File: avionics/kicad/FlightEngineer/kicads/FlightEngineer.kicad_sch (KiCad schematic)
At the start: 142 parts

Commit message: feat(avionics): FlightEngineer schematic-first rebuild to ERC 0; PCB placed, DRC 31 open
Replaces FlightEngineer's legacy schematic/PCB (586 ERC violations, PCB pad
nets not matching the schematic at all, gen_flight_engineer.py itself confirmed
drifted per its own injector script's warning) with a fresh generator
pipeline matching Pilot/XO's method (gen_fe_sch.py / gen_fe_footprints.py /
gen_fe_pcb.py), transcribing every pin table from its own OEM datasheet.

Power path: TPS54620 x2 (dual-redundant diode-OR'd 5V BEC) + TPS54540 (6V
BEC), INA226 x5 (main bus + 4 ESC branches), BQ76930 6S cell monitor (Table
9-3 6-cell tap configuration). Trust module rebuilt to the CURRENT target per
FlightEngineer.md's own 2026-08-03 retarget note (MSPM0G3518-Q1 RHB-32 + real
SLB9672 + ISOW1044BDFMR + ISOW1412DFMR), not the superseded MSPM0G3507/
SLB9670 the old injector script still names; the RHB-32 pinmux is reused
verbatim from retarget_mspm0g351x_slb9672.py's own already-verified
FLIGHT_ENGINEER_REMAP/FLIGHT_ENGINEER_TPM_NETS tables rather than re-derived
from the 1500-line datasheet pin-attribute table. ISOW1412's EN/FLT pin is
now wired to a real MCU GPIO (RS485_FLT_N) instead of Pilot's hard-tied
convention, since the RHB-32 pinmux happened to free one.

One part-number defect found in FlightEngineer.md's own BOM and corrected
(flagged, not silently fixed): "AON6556" (Q_BATT_DSG, cited 60V/30A) does not
exist in AOSMD's catalog (their 30V AlphaMOS family tops out at AON6554/
6558; no 60V "6556" found) — substituted with AON6260, a real AOSMD 60V/85A
DFN5x6 MOSFET; NEEDS owner confirmation. MBRD1045CT and SMBJ33CA are
confirmed real via manufacturer/distributor catalog search but their
datasheet PDFs could not be fetched this pass (every mirror returned an HTML
block page) — standard package pinouts used, flagged for a follow-up fetch.

ERC 0 confirmed (kicad-cli sch erc --severity-all, 151 parts, 539 pins).

PCB: courtyard area was budgeted BEFORE layout per docs/solutions/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
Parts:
- removed C1, C2: Panasonic EEF-CX1V221R 220uF/35V, symbol C_Generic
- removed C3: 100nF X7R 0805 50V, symbol C_Generic
- removed CM1, CM2: Wurth 7440640500 10A 2x100uH, symbol CMC_7440640500
- removed CM_ESC1, CM_ESC2, CM_ESC3, CM_ESC4, CM_ESC5: Wurth 7440640500 10A 2x100uH per-ESC CMC, symbol CMC_7440640500
- removed C_5V_OUT: 100nF X7R 0805, symbol C_Generic
- removed C_BEC1_IN, C_BEC2_IN, C_BEC_SV_IN: 100uF/50V electrolytic, symbol C_Generic
- removed C_BEC1_OUT, C_BEC2_OUT, C_BEC_SV_OUT: 220uF 10V electrolytic + 100nF X7R, symbol C_Generic
- removed C_BOOT1, C_BOOT2, C_BOOT_SV: 100nF X7R (BOOT-SW), symbol C_Generic
- removed C_CAP: 4.7uF X7R 0603 BQ76930 boot cap, symbol C_Generic
- removed C_COMP2_SV, C_COMPB1, C_COMPB2: C comp2 hi-f pole (verify per TPS54620 DS), symbol C_Generic
- removed C_COMPA1, C_COMPA2, C_COMP_SV: C comp (verify per TPS54620 DS), symbol C_Generic
- removed C_DEC1, C_DEC2, C_DEC3, C_DEC4, C_DEC5: Panasonic EEUFC1V471 470uF/35V D10x20mm low-ESR, symbol C_Generic
- removed C_DM1: Wurth 885012207016 10uF/50V X7R 1210, symbol C_Generic
- removed C_H_ADM1, C_H_ADM2, C_H_ISO1, C_H_TPM1: 100nF, symbol C_Generic
- removed C_H_IN: 10uF, symbol C_Generic
- removed C_H_ISO2, C_H_VCORE: 1uF, symbol C_Generic
- removed C_H_OUT: 22uF, symbol C_Generic
- removed C_NTC: 100nF X7R 0805 BQ76930 TS1 filter, symbol C_Generic
- removed C_SS1, C_SS2, C_SS_SV: 10nF soft-start (verify per TPS54620 DS), symbol C_Generic
- removed C_Y1, C_Y2: Kemet SA305E472MAR 4.7nF/250V Y2, symbol C_Generic
- removed D1: SMBJ33CA 33V/400W TVS, symbol SMBJ33CA
- removed D_I2C: NXP PRTR5V0U2X Dual TVS 5V clamp I2C RF protection, symbol PRTR5V0U2X
- removed D_OR1, D_OR2: MBRD1045CT Dual Schottky 10A/45V, symbol MBRD1045CT
- removed F1: Littelfuse 0297150.ZXNV 150A MAXI, symbol Fuse_MAXI_150A
- removed FB_5V1, FB_5V2, FB_SERVO: Wurth 742792612 600R@100MHz 2A, symbol FB_Generic
- removed F_ESC1, F_ESC2, F_ESC3, F_ESC4, F_ESC5: Littelfuse 0297040.WXNV 40A mini blade, symbol Fuse_Mini_40A
- removed J_5V: Molex Nano-Fit 4P 2.5mm avionics bus, symbol Nano_Fit_4P
- removed J_ALERT: JST-GH SM02B-GHS-TB 2P 1.25mm ALERT to Wash GPIO, symbol Conn_JST_GH_02P
- removed J_BAL: JST XH-7P 2.54mm 6S balance lead, symbol JST_XH_7P
- removed J_BATT: Amass XT60PW-F, symbol XT60PW_F
- removed J_CAN_IN_H: CAN-FD trunk IN (CANH/CANL/GND), symbol Conn_JST_GH_03P
- removed J_CAN_OUT_H: CAN-FD trunk OUT (CANH/CANL/GND), symbol Conn_JST_GH_03P
- removed J_CHASSIS: M3 x8 brass standoff (x4), symbol M3_ChassisPad
- removed J_ESC1, J_ESC2, J_ESC3, J_ESC4, J_ESC5: Amass XT30PW-F PCB-mount XT30 female, symbol XT30PW_F
- removed J_I2C: JST-GH SM04B-GHS-TB 4P 1.25mm PDB I2C to FC1, symbol Conn_JST_GH_04P
- removed J_NTC: JST-GH 2P 1.25mm battery NTC thermistor input, symbol Conn_JST_GH_02P
- removed J_PGND_BATT: M3 chassis lug, symbol M3_ChassisPad
- removed J_RS485_IN_H: RS-485 trunk IN (A/B/GND), symbol Conn_JST_GH_03P
- removed J_RS485_OUT_H: RS-485 trunk OUT (A/B/GND), symbol Conn_JST_GH_03P
- removed J_SERVO_5V: Molex Nano-Fit 4P 2.5mm SERVO-5V bus, symbol Nano_Fit_4P
- removed J_SHLD_5V: PGND via-pad 1.2mm for 5V cable shield, symbol M3_ChassisPad
- removed J_SHLD_ALERT: PGND via-pad ALERT cable shield, symbol M3_ChassisPad
- removed J_SHLD_ESC1, J_SHLD_ESC2, J_SHLD_ESC3, J_SHLD_ESC4, J_SHLD_ESC5: M3 chassis lug for ESC cable shield, symbol M3_ChassisPad
- removed J_SHLD_I2C: PGND via-pad I2C cable shield, symbol M3_ChassisPad
- removed J_SHLD_NTC: PGND via-pad NTC cable shield, symbol M3_ChassisPad
- removed J_SHLD_SV: PGND via-pad for SERVO-5V cable shield, symbol M3_ChassisPad
- removed J_SWD_H: SWD: DIO/CLK/NRST/GND, symbol Conn_JST_GH_04P
- removed L1, L2, L4: Wurth 744314100 10uH >=6A Isat, symbol L_Generic
- removed L_H1: 2.2uH, symbol L_Generic
- removed Q_BATT_DSG: AON6556 60V/30A NMOS, symbol AON6556
- removed RS1, RS2, RS3, RS4, RS5, RS_MAIN: Bourns CSS2H-2512K-1L00F 1mOhm 3W, symbol CSS2H_2512K_1mOhm
- removed R_ALERT: 2.2k 0402 ALERT pull-up to +5V, symbol R_Generic
- removed R_BAL1, R_BAL2, R_BAL3, R_BAL4, R_BAL5, R_BAL6: 100R 0402 balance lead protection resistor, symbol R_Generic
- removed R_CHGND: 0R 0402 (chassis-PGND bond, configurable), symbol R_Generic
- removed R_COMP1, R_COMP2, R_COMP_SV: R comp (verify per TPS54620 DS), symbol R_Generic
- removed R_DSG_G: 10k 0402, symbol R_Generic
- removed R_FB1_1, R_FB2_1: R for Vout=5.3V (top), symbol R_Generic
- removed R_FB1_2, R_FB2_2: R for Vout=5.3V (bot), symbol R_Generic
- removed R_FBSV_1: R for Vout=5.0V (top), symbol R_Generic
- removed R_FBSV_2: R for Vout=5.0V (bot), symbol R_Generic
- removed R_H_485TERM, R_H_CANTERM: 120R, symbol R_Generic
- removed R_H_FBB: 20k, symbol R_Generic
- removed R_H_FBT, R_H_NRST, R_H_TPM_RST: 10k, symbol R_Generic
- removed R_VSNS: 0R Kelvin VBUS tap (VDIS), symbol R_Generic
- removed SJ_H_485, SJ_H_CAN: open by default, Jumper:SolderJumper-2_P1.3mm_Open_Pad1.0x1.5mm, symbol SJ_Generic
- removed U_BEC_5V_1, U_BEC_5V_2: TPS54620RGYT 6A/28V sync buck 5.3Vout, symbol TPS54620RGYT
- removed U_BEC_SERVO_5V: TPS54620RGYT 6A/28V sync buck 5.0V servo rail, symbol TPS54620RGYT
- removed U_CELL: BQ76930PWRQ1 6S cell monitor + HW protection, symbol BQ76930PWRQ1
- removed U_IS1: INA226AIDGSR I2C addr=0x40, symbol INA226AIDGSR
- removed U_IS2: INA226AIDGSR I2C addr=0x41, symbol INA226AIDGSR
- removed U_IS3: INA226AIDGSR I2C addr=0x42, symbol INA226AIDGSR
- removed U_IS4: INA226AIDGSR I2C addr=0x43, symbol INA226AIDGSR
- removed U_IS5: INA226AIDGSR I2C addr=0x45, symbol INA226AIDGSR
- removed U_ISOCAN: TI ISOW1044BDFMR, Package_SO:SOIC-20W_7.5x12.8mm_P1.27mm, symbol Observer_ISOW1044BDFMR
- removed U_IS_MAIN: INA226AIDGSR I2C addr=0x44, symbol INA226AIDGSR
- removed U_MCU: TI MSPM0G3518-Q1, Package_DFN_QFN:Texas_RHB0032E_VQFN-32-1EP_5x5mm_P0.5mm_EP3.45x3.45mm, symbol MSPM0G3518_Q1_RHB
- removed U_REG_3V3_H: TLV62569DBVR -> +3V3, symbol TLV62569_DBV_H
- removed U_RS485: TI ISOW1412, Package_SO:SOIC-20W_7.5x12.8mm_P1.27mm, symbol GW_ISOW1412
- removed U_TPM: Infineon SLB 9672AU2.0, Package_DFN_QFN:QFN-32-1EP_5x5mm_P0.5mm_EP3.6x3.6mm, symbol SLB9672_TPM
- added C1: 220uF 35V, Capacitor_THT:CP_Radial_D10.0mm_P5.00mm, symbol FlightEngineer:S_C1
- added C2: 220uF 35V, Capacitor_THT:CP_Radial_D10.0mm_P5.00mm, symbol FlightEngineer:S_C2
- added C3: 100nF X7R 0805, Capacitor_SMD:C_0805_2012Metric, symbol FlightEngineer:S_C3
- added CM1: 7440640500, Serenity-Custom:Wurth_7440640500_CMC_THT, symbol FlightEngineer:S_CM1
- added CM2: 7440640500, Serenity-Custom:Wurth_7440640500_CMC_THT, symbol FlightEngineer:S_CM2
- added CM_ESC1: 7440640500, Serenity-Custom:Wurth_7440640500_CMC_THT, symbol FlightEngineer:S_CM_ESC1
- added CM_ESC2: 7440640500, Serenity-Custom:Wurth_7440640500_CMC_THT, symbol FlightEngineer:S_CM_ESC2
- added CM_ESC3: 7440640500, Serenity-Custom:Wurth_7440640500_CMC_THT, symbol FlightEngineer:S_CM_ESC3
- added CM_ESC4: 7440640500, Serenity-Custom:Wurth_7440640500_CMC_THT, symbol FlightEngineer:S_CM_ESC4
- added C_BEC1_BOOT: 100nF, Capacitor_SMD:C_0402_1005Metric, symbol FlightEngineer:S_C_BEC1_BOOT
- added C_BEC1_COMP: 2.2nF, Capacitor_SMD:C_0402_1005Metric, symbol FlightEngineer:S_C_BEC1_COMP
- added C_BEC1_IN: 100uF 50V, Capacitor_SMD:C_1210_3225Metric, symbol FlightEngineer:S_C_BEC1_IN
- added C_BEC1_OUT1: 220uF, Capacitor_SMD:C_1210_3225Metric, symbol FlightEngineer:S_C_BEC1_OUT1
- added C_BEC1_OUT2: 100nF, Capacitor_SMD:C_0402_1005Metric, symbol FlightEngineer:S_C_BEC1_OUT2
- added C_BEC1_SS: 10nF, Capacitor_SMD:C_0402_1005Metric, symbol FlightEngineer:S_C_BEC1_SS
- added C_BEC2_BOOT: 100nF, Capacitor_SMD:C_0402_1005Metric, symbol FlightEngineer:S_C_BEC2_BOOT
- added C_BEC2_COMP: 2.2nF, Capacitor_SMD:C_0402_1005Metric, symbol FlightEngineer:S_C_BEC2_COMP
- added C_BEC2_IN: 100uF 50V, Capacitor_SMD:C_1210_3225Metric, symbol FlightEngineer:S_C_BEC2_IN
- added C_BEC2_OUT1: 220uF, Capacitor_SMD:C_1210_3225Metric, symbol FlightEngineer:S_C_BEC2_OUT1
- added C_BEC2_OUT2: 100nF, Capacitor_SMD:C_0402_1005Metric, symbol FlightEngineer:S_C_BEC2_OUT2
- added C_BEC2_SS: 10nF, Capacitor_SMD:C_0402_1005Metric, symbol FlightEngineer:S_C_BEC2_SS
- added C_BEC6_BOOT: 100nF, Capacitor_SMD:C_0402_1005Metric, symbol FlightEngineer:S_C_BEC6_BOOT
- added C_BEC6_COMP: 1nF, Capacitor_SMD:C_0402_1005Metric, symbol FlightEngineer:S_C_BEC6_COMP
- added C_BEC_SV_IN: 100uF 50V, Capacitor_SMD:C_1210_3225Metric, symbol FlightEngineer:S_C_BEC_SV_IN
- added C_BEC_SV_OUT1: 100uF, Capacitor_SMD:C_1210_3225Metric, symbol FlightEngineer:S_C_BEC_SV_OUT1
- added C_BEC_SV_OUT2: 100nF, Capacitor_SMD:C_0402_1005Metric, symbol FlightEngineer:S_C_BEC_SV_OUT2
- added C_CAP1: 0.1uF, Capacitor_SMD:C_0402_1005Metric, symbol FlightEngineer:S_C_CAP1
- added C_CAP2: 0.1uF, Capacitor_SMD:C_0402_1005Metric, symbol FlightEngineer:S_C_CAP2
- added C_DEC1: 470uF 35V low-ESR, Capacitor_THT:CP_Radial_D10.0mm_P5.00mm, symbol FlightEngineer:S_C_DEC1
- added C_DEC2: 470uF 35V low-ESR, Capacitor_THT:CP_Radial_D10.0mm_P5.00mm, symbol FlightEngineer:S_C_DEC2
- added C_DEC3: 470uF 35V low-ESR, Capacitor_THT:CP_Radial_D10.0mm_P5.00mm, symbol FlightEngineer:S_C_DEC3
- added C_DEC4: 470uF 35V low-ESR, Capacitor_THT:CP_Radial_D10.0mm_P5.00mm, symbol FlightEngineer:S_C_DEC4
- added C_DM1: 10uF 50V X7R 1210, Capacitor_SMD:C_1210_3225Metric, symbol FlightEngineer:S_C_DM1
- added C_H_IN: 10uF, Capacitor_SMD:C_0805_2012Metric, symbol FlightEngineer:S_C_H_IN
- added C_H_OUT: 22uF, Capacitor_SMD:C_0805_2012Metric, symbol FlightEngineer:S_C_H_OUT
- added C_ISOCAN1: 10nF, Capacitor_SMD:C_0402_1005Metric, symbol FlightEngineer:S_C_ISOCAN1
- added C_ISOCAN2: 10uF, Capacitor_SMD:C_0805_2012Metric, symbol FlightEngineer:S_C_ISOCAN2
- added C_ISOCAN3: 100nF, Capacitor_SMD:C_0402_1005Metric, symbol FlightEngineer:S_C_ISOCAN3
- added C_ISOCAN4: 10nF, Capacitor_SMD:C_0402_1005Metric, symbol FlightEngineer:S_C_ISOCAN4
- added C_ISOCAN5: 10uF, Capacitor_SMD:C_0805_2012Metric, symbol FlightEngineer:S_C_ISOCAN5
- added C_MCU_3V3: 100nF, Capacitor_SMD:C_0402_1005Metric, symbol FlightEngineer:S_C_MCU_3V3
- added C_MCU_VCORE: 1uF, Capacitor_SMD:C_0402_1005Metric, symbol FlightEngineer:S_C_MCU_VCORE
- added C_NTC: 100nF X7R, Capacitor_SMD:C_0402_1005Metric, symbol FlightEngineer:S_C_NTC
- added C_REGOUT: 1uF, Capacitor_SMD:C_0402_1005Metric, symbol FlightEngineer:S_C_REGOUT
- added C_RS485_1: 10nF, Capacitor_SMD:C_0402_1005Metric, symbol FlightEngineer:S_C_RS485_1
- added C_RS485_2: 10uF, Capacitor_SMD:C_0805_2012Metric, symbol FlightEngineer:S_C_RS485_2
- added C_RS485_3: 100nF, Capacitor_SMD:C_0402_1005Metric, symbol FlightEngineer:S_C_RS485_3
- added C_RS485_4: 10nF, Capacitor_SMD:C_0402_1005Metric, symbol FlightEngineer:S_C_RS485_4
- added C_RS485_5: 10uF, Capacitor_SMD:C_0805_2012Metric, symbol FlightEngineer:S_C_RS485_5
- added C_TPM1: 1uF, Capacitor_SMD:C_0402_1005Metric, symbol FlightEngineer:S_C_TPM1
- added C_TPM2: 100nF, Capacitor_SMD:C_0402_1005Metric, symbol FlightEngineer:S_C_TPM2
- added C_TPM3: 100nF, Capacitor_SMD:C_0402_1005Metric, symbol FlightEngineer:S_C_TPM3
- added C_TPM4: 100nF, Capacitor_SMD:C_0402_1005Metric, symbol FlightEngineer:S_C_TPM4
- added C_Y1: 4.7nF 250V Y2, Capacitor_SMD:C_0805_2012Metric, symbol FlightEngineer:S_C_Y1
- added C_Y2: 4.7nF 250V Y2, Capacitor_SMD:C_0805_2012Metric, symbol FlightEngineer:S_C_Y2
- added D1: SMBJ33CA, Diode_SMD:D_SMB, symbol FlightEngineer:S_D1
- added D_I2C: PRTR5V0U2X, Package_TO_SOT_SMD:SOT-363_SC-70-6, symbol FlightEngineer:S_D_I2C
- added D_OR1: MBRD1045CT, Package_TO_SOT_SMD:TO-263-3_TabPin2, symbol FlightEngineer:S_D_OR1
- added D_OR2: MBRD1045CT, Package_TO_SOT_SMD:TO-263-3_TabPin2, symbol FlightEngineer:S_D_OR2
- added ESC1_LINK: 0R link, Resistor_SMD:R_0603_1608Metric, symbol FlightEngineer:S_ESC1_LINK
- added ESC2_LINK: 0R link, Resistor_SMD:R_0603_1608Metric, symbol FlightEngineer:S_ESC2_LINK
- added ESC3_LINK: 0R link, Resistor_SMD:R_0603_1608Metric, symbol FlightEngineer:S_ESC3_LINK
- added ESC4_LINK: 0R link, Resistor_SMD:R_0603_1608Metric, symbol FlightEngineer:S_ESC4_LINK
- added F1: 0297150.ZXNV 150A MAXI, Serenity-Custom:MAXI_Blade_Fuseholder_2P, symbol FlightEngineer:S_F1
- added FB_5V1: 742792612, Inductor_SMD:L_1210_3225Metric, symbol FlightEngineer:S_FB_5V1
- added FB_5V2: 742792612, Inductor_SMD:L_1210_3225Metric, symbol FlightEngineer:S_FB_5V2
- added FB_6V: 742792612, Inductor_SMD:L_1210_3225Metric, symbol FlightEngineer:S_FB_6V
- added F_ESC1: 0297040.WXNV 40A mini, Fuse:Fuseholder_Blade_Mini_Keystone_3568, symbol FlightEngineer:S_F_ESC1
- added F_ESC2: 0297040.WXNV 40A mini, Fuse:Fuseholder_Blade_Mini_Keystone_3568, symbol FlightEngineer:S_F_ESC2
- added F_ESC3: 0297040.WXNV 40A mini, Fuse:Fuseholder_Blade_Mini_Keystone_3568, symbol FlightEngineer:S_F_ESC3
- added F_ESC4: 0297040.WXNV 40A mini, Fuse:Fuseholder_Blade_Mini_Keystone_3568, symbol FlightEngineer:S_F_ESC4
- added J_485_IN: SM03B-GHS-TB, Connector_JST:JST_GH_SM03B-GHS-TB_1x03-1MP_P1.25mm_Horizontal, symbol FlightEngineer:S_J_485_IN
- added J_485_OUT: SM03B-GHS-TB, Connector_JST:JST_GH_SM03B-GHS-TB_1x03-1MP_P1.25mm_Horizontal, symbol FlightEngineer:S_J_485_OUT
- added J_5V: Nano-Fit 4P, Connector_Molex:Molex_Nano-Fit_105309-xx04_1x04_P2.50mm_Vertical, symbol FlightEngineer:S_J_5V
- added J_6V: Nano-Fit 4P, Connector_Molex:Molex_Nano-Fit_105309-xx04_1x04_P2.50mm_Vertical, symbol FlightEngineer:S_J_6V
- added J_ALERT: SM02B-GHS-TB, Connector_JST:JST_GH_SM02B-GHS-TB_1x02-1MP_P1.25mm_Horizontal, symbol FlightEngineer:S_J_ALERT
- added J_BAL: XH-7P, Connector_JST:JST_XH_B7B-XH-A_1x07_P2.50mm_Vertical, symbol FlightEngineer:S_J_BAL
- added J_BATT: XT60PW-F, Connector_AMASS:AMASS_XT60PW-F_1x02_P7.20mm_Horizontal, symbol FlightEngineer:S_J_BATT
- added J_CAN_IN: SM03B-GHS-TB, Connector_JST:JST_GH_SM03B-GHS-TB_1x03-1MP_P1.25mm_Horizontal, symbol FlightEngineer:S_J_CAN_IN
- added J_CAN_OUT: SM03B-GHS-TB, Connector_JST:JST_GH_SM03B-GHS-TB_1x03-1MP_P1.25mm_Horizontal, symbol FlightEngineer:S_J_CAN_OUT
- added J_CHASSIS: M3 standoff x4, Serenity-Custom:M3_Chassis_Lug_PGND, symbol FlightEngineer:S_J_CHASSIS
- added J_ESC1: XT30PW-F, Connector_AMASS:AMASS_XT30PW-F_1x02_P2.50mm_Horizontal, symbol FlightEngineer:S_J_ESC1
- added J_ESC2: XT30PW-F, Connector_AMASS:AMASS_XT30PW-F_1x02_P2.50mm_Horizontal, symbol FlightEngineer:S_J_ESC2
- added J_ESC3: XT30PW-F, Connector_AMASS:AMASS_XT30PW-F_1x02_P2.50mm_Horizontal, symbol FlightEngineer:S_J_ESC3
- added J_ESC4: XT30PW-F, Connector_AMASS:AMASS_XT30PW-F_1x02_P2.50mm_Horizontal, symbol FlightEngineer:S_J_ESC4
- added J_I2C: SM04B-GHS-TB, Connector_JST:JST_GH_SM04B-GHS-TB_1x04-1MP_P1.25mm_Horizontal, symbol FlightEngineer:S_J_I2C
- added J_NTC: SM02B-GHS-TB, Connector_JST:JST_GH_SM02B-GHS-TB_1x02-1MP_P1.25mm_Horizontal, symbol FlightEngineer:S_J_NTC
- added J_PGND_BATT: M3 chassis lug, Serenity-Custom:M3_Chassis_Lug_PGND, symbol FlightEngineer:S_J_PGND_BATT
- added J_SHLD_5V: PGND via, Serenity-Custom:PGND_ViaPad_1p2mm, symbol FlightEngineer:S_J_SHLD_5V
- added J_SHLD_6V: PGND via, Serenity-Custom:PGND_ViaPad_1p2mm, symbol FlightEngineer:S_J_SHLD_6V
- added J_SHLD_ALERT: PGND via, Serenity-Custom:PGND_ViaPad_1p2mm, symbol FlightEngineer:S_J_SHLD_ALERT
- added J_SHLD_ESC1: M3 chassis lug, Serenity-Custom:M3_Chassis_Lug_PGND, symbol FlightEngineer:S_J_SHLD_ESC1
- added J_SHLD_ESC2: M3 chassis lug, Serenity-Custom:M3_Chassis_Lug_PGND, symbol FlightEngineer:S_J_SHLD_ESC2
- added J_SHLD_ESC3: M3 chassis lug, Serenity-Custom:M3_Chassis_Lug_PGND, symbol FlightEngineer:S_J_SHLD_ESC3
- added J_SHLD_ESC4: M3 chassis lug, Serenity-Custom:M3_Chassis_Lug_PGND, symbol FlightEngineer:S_J_SHLD_ESC4
- added J_SHLD_I2C: PGND via, Serenity-Custom:PGND_ViaPad_1p2mm, symbol FlightEngineer:S_J_SHLD_I2C
- added J_SHLD_NTC: PGND via, Serenity-Custom:PGND_ViaPad_1p2mm, symbol FlightEngineer:S_J_SHLD_NTC
- added J_SWD_H: SM04B-GHS-TB, Connector_JST:JST_GH_SM04B-GHS-TB_1x04-1MP_P1.25mm_Horizontal, symbol FlightEngineer:S_J_SWD_H
- added L1: 10uH 6A, Inductor_SMD:L_1210_3225Metric, symbol FlightEngineer:S_L1
- added L2: 10uH 6A, Inductor_SMD:L_1210_3225Metric, symbol FlightEngineer:S_L2
- added L3: 10uH 6A, Inductor_SMD:L_1210_3225Metric, symbol FlightEngineer:S_L3
- added L_H1: 2.2uH, Inductor_SMD:L_1210_3225Metric, symbol FlightEngineer:S_L_H1
- added Q_BATT_CHG: AON6260 (DNP), Serenity-Custom:AOSMD_DFN5x6-8L, symbol FlightEngineer:S_Q_BATT_CHG
- added Q_BATT_DSG: AON6260, Serenity-Custom:AOSMD_DFN5x6-8L, symbol FlightEngineer:S_Q_BATT_DSG
- added RS1: 1mOhm 3W Kelvin, Resistor_SMD:R_Shunt_Vishay_WSK2512_6332Metric_T1.19mm, symbol FlightEngineer:S_RS1
- added RS2: 1mOhm 3W Kelvin, Resistor_SMD:R_Shunt_Vishay_WSK2512_6332Metric_T1.19mm, symbol FlightEngineer:S_RS2
- added RS3: 1mOhm 3W Kelvin, Resistor_SMD:R_Shunt_Vishay_WSK2512_6332Metric_T1.19mm, symbol FlightEngineer:S_RS3
- added RS4: 1mOhm 3W Kelvin, Resistor_SMD:R_Shunt_Vishay_WSK2512_6332Metric_T1.19mm, symbol FlightEngineer:S_RS4
- added RS_MAIN: 1mOhm 5W Kelvin, Resistor_SMD:R_Shunt_Vishay_WSK2512_6332Metric_T1.19mm, symbol FlightEngineer:S_RS_MAIN
- added R_485TERM: 120R, Resistor_SMD:R_0603_1608Metric, symbol FlightEngineer:S_R_485TERM
- added R_ALERT: 2.2k, Resistor_SMD:R_0402_1005Metric, symbol FlightEngineer:S_R_ALERT
- added R_BAL1: 100R, Resistor_SMD:R_0402_1005Metric, symbol FlightEngineer:S_R_BAL1
- added R_BAL2: 100R, Resistor_SMD:R_0402_1005Metric, symbol FlightEngineer:S_R_BAL2
- added R_BAL3: 100R, Resistor_SMD:R_0402_1005Metric, symbol FlightEngineer:S_R_BAL3
- added R_BAL4: 100R, Resistor_SMD:R_0402_1005Metric, symbol FlightEngineer:S_R_BAL4
- added R_BAL5: 100R, Resistor_SMD:R_0402_1005Metric, symbol FlightEngineer:S_R_BAL5
- added R_BAL6: 100R, Resistor_SMD:R_0402_1005Metric, symbol FlightEngineer:S_R_BAL6
- added R_CANSTB: 0R, Resistor_SMD:R_0402_1005Metric, symbol FlightEngineer:S_R_CANSTB
- added R_CANTERM: 120R, Resistor_SMD:R_0603_1608Metric, symbol FlightEngineer:S_R_CANTERM
- added R_CHGND: 0R socketed, Resistor_SMD:R_0402_1005Metric, symbol FlightEngineer:S_R_CHGND
- added R_DSG_G: 10k, Resistor_SMD:R_0402_1005Metric, symbol FlightEngineer:S_R_DSG_G
- added R_EN_BIAS: 100k, Resistor_SMD:R_0402_1005Metric, symbol FlightEngineer:S_R_EN_BIAS
- added R_FB1_1: 56.2k 1%, Resistor_SMD:R_0402_1005Metric, symbol FlightEngineer:S_R_FB1_1
- added R_FB1_2: 10.0k 1%, Resistor_SMD:R_0402_1005Metric, symbol FlightEngineer:S_R_FB1_2
- added R_FB2_1: 56.2k 1%, Resistor_SMD:R_0402_1005Metric, symbol FlightEngineer:S_R_FB2_1
- added R_FB2_2: 10.0k 1%, Resistor_SMD:R_0402_1005Metric, symbol FlightEngineer:S_R_FB2_2
- added R_FB6_1: 64.9k 1%, Resistor_SMD:R_0402_1005Metric, symbol FlightEngineer:S_R_FB6_1
- added R_FB6_2: 10.0k 1%, Resistor_SMD:R_0402_1005Metric, symbol FlightEngineer:S_R_FB6_2
- added R_GND_PGND: 0R, Resistor_SMD:R_0603_1608Metric, symbol FlightEngineer:S_R_GND_PGND
- added R_I2C_SCL: 4.7k, Resistor_SMD:R_0402_1005Metric, symbol FlightEngineer:S_R_I2C_SCL
- added R_I2C_SDA: 4.7k, Resistor_SMD:R_0402_1005Metric, symbol FlightEngineer:S_R_I2C_SDA
- added R_MCU_NRST: 10k, Resistor_SMD:R_0402_1005Metric, symbol FlightEngineer:S_R_MCU_NRST
- added R_NTC_PU: 10k, Resistor_SMD:R_0402_1005Metric, symbol FlightEngineer:S_R_NTC_PU
- added R_RS485FLT_PU: 10k, Resistor_SMD:R_0402_1005Metric, symbol FlightEngineer:S_R_RS485FLT_PU
- added R_TPM10: 10k, Resistor_SMD:R_0402_1005Metric, symbol FlightEngineer:S_R_TPM10
- added R_TPMCS: 10k, Resistor_SMD:R_0402_1005Metric, symbol FlightEngineer:S_R_TPMCS
- added U_BEC_5V_1: TPS54620RGYT, Serenity-Custom:Texas_RGY0014A_VQFN-14-1EP_3.5x3.5mm, symbol FlightEngineer:S_U_BEC_5V_1
- added U_BEC_5V_2: TPS54620RGYT, Serenity-Custom:Texas_RGY0014A_VQFN-14-1EP_3.5x3.5mm, symbol FlightEngineer:S_U_BEC_5V_2
- added U_BEC_6V: TPS54540DDAR, Package_SO:TI_SO-PowerPAD-8, symbol FlightEngineer:S_U_BEC_6V
- added U_CELL: BQ76930PWRQ1, Package_SO:TSSOP-30_4.4x7.8mm_P0.5mm, symbol FlightEngineer:S_U_CELL
- added U_IS1: INA226AIDGSR, Package_SO:VSSOP-10_3x3mm_P0.5mm, symbol FlightEngineer:S_U_IS1
- added U_IS2: INA226AIDGSR, Package_SO:VSSOP-10_3x3mm_P0.5mm, symbol FlightEngineer:S_U_IS2
- added U_IS3: INA226AIDGSR, Package_SO:VSSOP-10_3x3mm_P0.5mm, symbol FlightEngineer:S_U_IS3
- added U_IS4: INA226AIDGSR, Package_SO:VSSOP-10_3x3mm_P0.5mm, symbol FlightEngineer:S_U_IS4
- added U_ISOCAN: ISOW1044BDFMR, Package_SO:SOIC-20W_7.5x12.8mm_P1.27mm, symbol FlightEngineer:S_U_ISOCAN
- added U_IS_MAIN: INA226AIDGSR, Package_SO:VSSOP-10_3x3mm_P0.5mm, symbol FlightEngineer:S_U_IS_MAIN
- added U_MCU: MSPM0G3518-Q1, Package_DFN_QFN:Texas_RHB0032E_VQFN-32-1EP_5x5mm_P0.5mm_EP3.45x3.45mm, symbol FlightEngineer:S_U_MCU
- added U_REG_3V3_H: TLV62569DBVR, Package_TO_SOT_SMD:SOT-23, symbol FlightEngineer:S_U_REG_3V3_H
- added U_RS485: ISOW1412DFMR, Package_SO:SOIC-20W_7.5x12.8mm_P1.27mm, symbol FlightEngineer:S_U_RS485
- added U_TPM: SLB9672XU20, Package_DFN_QFN:QFN-32-1EP_5x5mm_P0.5mm_EP3.6x3.6mm, symbol FlightEngineer:S_U_TPM
- added VDIS_LINK: 0R link, Resistor_SMD:R_0603_1608Metric, symbol FlightEngineer:S_VDIS_LINK
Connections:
- net +3V3: now also C_H_OUT.1 (P), C_ISOCAN3.1 (P), C_MCU_3V3.1 (P), C_RS485_3.1 (P), C_TPM1.1 (P), C_TPM2.1 (P), C_TPM3.1 (P), C_TPM4.1 (P), L_H1.2 (B), R_MCU_NRST.1 (A), R_RS485FLT_PU.1 (A), R_TPM10.1 (A), R_TPMCS.1 (A), U_ISOCAN.1 (VIO), U_MCU.4 (+3V3), U_REG_3V3_H.1 (EN), U_REG_3V3_H.5 (FB), U_RS485.1 (VIO), U_TPM.1 (VDD), U_TPM.14 (VDD), U_TPM.22 (VDD)
- net +5V: now also C_H_IN.1 (P), C_ISOCAN1.1 (P), C_ISOCAN2.1 (P), C_RS485_1.1 (P), C_RS485_2.1 (P), D_I2C.5 (VCC), J_I2C.2 (+5V), R_ALERT.1 (A), R_I2C_SCL.1 (A), R_I2C_SDA.1 (A), U_IS1.6 (VS), U_IS2.2 (A0), U_IS2.6 (VS), U_IS3.6 (VS), U_IS4.6 (VS), U_ISOCAN.9 (VDD), U_IS_MAIN.1 (A1), U_IS_MAIN.6 (VS), U_REG_3V3_H.4 (VIN), U_RS485.9 (VDD)
- net CANFD_RX: now also U_ISOCAN.5 (RXD), U_MCU.17 (PA13/CAN0_RX)
- net CANFD_TX: now also U_ISOCAN.3 (TXD), U_MCU.16 (PA12/CAN0_TX)
- net CAN_H: now also J_CAN_IN.1 (H), J_CAN_OUT.1 (H), R_CANTERM.1 (A), U_ISOCAN.19 (CANH)
- net CAN_L: now also J_CAN_IN.2 (L), J_CAN_OUT.2 (L), R_CANTERM.2 (B), U_ISOCAN.18 (CANL)
- net ESC1_FUSED: now also CM_ESC1.1 (P1A), C_DEC1.1 (P), F_ESC1.2 (B)
- net ESC2_FUSED: now also CM_ESC2.1 (P1A), C_DEC2.1 (P), F_ESC2.2 (B)
- net ESC3_FUSED: now also CM_ESC3.1 (P1A), C_DEC3.1 (P), F_ESC3.2 (B)
- net ESC4_FUSED: now also CM_ESC4.1 (P1A), C_DEC4.1 (P), F_ESC4.2 (B)
- net ISO_5V_CAN: now also C_ISOCAN4.1 (P), C_ISOCAN5.1 (P), U_ISOCAN.12 (VISOOUT), U_ISOCAN.13 (VSIN), U_ISOCAN.20 (VISOIN)
- net ISO_GND_485: now also C_RS485_4.2 (N), C_RS485_5.2 (N), J_485_IN.3 (GND), J_485_OUT.3 (GND), U_RS485.11 (GND2), U_RS485.13 (MODE), U_RS485.15 (GISOIN)
- net ISO_GND_CAN: now also C_ISOCAN4.2 (N), C_ISOCAN5.2 (N), J_CAN_IN.3 (GND), J_CAN_OUT.3 (GND), U_ISOCAN.11 (GND2), U_ISOCAN.15 (GISOIN), U_ISOCAN.16 (GISOIN), U_ISOCAN.17 (GISOIN)
- net MCU_NRST: now also J_SWD_H.3 (NRST), R_MCU_NRST.2 (B), U_MCU.3 (NRST)
- net MCU_SWCLK: now also J_SWD_H.2 (CLK), U_MCU.24 (PA21b/SWCLK)
- net MCU_SWDIO: now also J_SWD_H.1 (DIO), U_MCU.23 (PA20/SWDIO)
- net MCU_VCORE: now also C_MCU_VCORE.1 (P), U_MCU.32 (VCORE)
- net NTC_P: now also C_NTC.1 (P), J_NTC.1 (NTC+), R_NTC_PU.2 (B), U_CELL.6 (TS1)
- net PGND: now also C1.2 (N), C2.2 (N), C3.2 (N), CM2.4 (P2B), CM_ESC1.3 (P2A), CM_ESC1.4 (P2B), CM_ESC2.3 (P2A), CM_ESC2.4 (P2B), CM_ESC3.3 (P2A), CM_ESC3.4 (P2B), CM_ESC4.3 (P2A), CM_ESC4.4 (P2B), C_DEC1.2 (N), C_DEC2.2 (N), C_DEC3.2 (N), C_DEC4.2 (N), C_DM1.2 (N), C_H_IN.2 (N), C_H_OUT.2 (N), C_MCU_3V3.2 (N), C_MCU_VCORE.2 (N), C_NTC.2 (N), C_Y2.1 (P), D1.2 (K), D_I2C.2 (GND), J_ALERT.1 (GND), J_ESC1.2 (-), J_ESC2.2 (-), J_ESC3.2 (-), J_ESC4.2 (-), J_I2C.1 (GND), J_NTC.2 (NTC-), J_PGND_BATT.1 (PGND), J_SHLD_5V.1 (PGND), J_SHLD_6V.1 (PGND), J_SHLD_ALERT.1 (PGND), J_SHLD_ESC1.1 (PGND), J_SHLD_ESC2.1 (PGND), J_SHLD_ESC3.1 (PGND), J_SHLD_ESC4.1 (PGND), J_SHLD_I2C.1 (PGND), J_SHLD_NTC.1 (PGND), J_SWD_H.4 (GND), R_CHGND.2 (B), R_GND_PGND.2 (B), U_CELL.13 (TS2), U_CELL.3 (VSS), U_MCU.33 (EP), U_MCU.5 (GND), U_REG_3V3_H.2 (GND), U_TPM.16 (NCI/GND), U_TPM.2 (GND), U_TPM.23 (GND), U_TPM.32 (GND), U_TPM.33 (EP), U_TPM.9 (GND)
- net RS485_A: now also J_485_IN.1 (A), J_485_OUT.1 (A), R_485TERM.1 (A), U_RS485.17 (Y), U_RS485.20 (A)
- net RS485_B: now also J_485_IN.2 (B), J_485_OUT.2 (B), R_485TERM.2 (B), U_RS485.18 (Z), U_RS485.19 (B)
- net RS485_DE: now also U_MCU.25 (PA21/GPIO), U_RS485.3 (DE), U_RS485.5 (RE)
- net RS485_FLT_N: now also R_RS485FLT_PU.2 (B), U_MCU.26 (PA22/GPIO), U_RS485.8 (EN/FLT)
- net RS485_RX: now also U_MCU.13 (PA9/UART1_RX), U_RS485.4 (R)
- net RS485_TX: now also U_MCU.12 (PA8/UART1_TX), U_RS485.2 (D)
- net TPM_PIRQ: now also U_MCU.7 (PA3/GPIO), U_TPM.18 (PIRQ#)
- net TPM_RESET_N: now also U_MCU.11 (PA7/GPIO), U_TPM.17 (RST#)
- net TPM_SPI_CS: now also R_TPMCS.2 (B), U_MCU.6 (PA2/SPI0_CS), U_TPM.20 (CS#)
- net TPM_SPI_MISO: now also U_MCU.8 (PA4/SPI0_MISO), U_TPM.24 (MISO)
- net TPM_SPI_MOSI: now also U_MCU.9 (PA5/SPI0_MOSI), U_TPM.21 (MOSI)
- net TPM_SPI_SCK: now also U_MCU.10 (PA6/SPI0_SCK), U_TPM.19 (SCLK)
- net VBAT: now also CM2.2 (P1B), F1.1 (A), Q_BATT_CHG.1 (S), Q_BATT_CHG.2 (S), Q_BATT_CHG.3 (S), Q_BATT_CHG.5 (D), Q_BATT_CHG.6 (D), Q_BATT_CHG.7 (D), Q_BATT_CHG.8 (D), Q_BATT_DSG.5 (D), Q_BATT_DSG.6 (D), Q_BATT_DSG.7 (D), Q_BATT_DSG.8 (D), U_CELL.15 (BAT), U_CELL.9 (REGSRC)
- net VDIS: now also FB_5V1.1 (IN), FB_5V2.1 (IN), FB_6V.1 (IN), F_ESC1.1 (A), F_ESC2.1 (A), F_ESC3.1 (A), F_ESC4.1 (A), Q_BATT_DSG.1 (S), Q_BATT_DSG.2 (S), Q_BATT_DSG.3 (S), R_EN_BIAS.1 (A), U_BEC_5V_1.4 (PVIN), U_BEC_5V_1.5 (PVIN), U_BEC_5V_1.6 (VIN), U_BEC_5V_2.4 (PVIN), U_BEC_5V_2.5 (PVIN), U_BEC_5V_2.6 (VIN), U_BEC_6V.2 (VIN), U_IS1.8 (VBUS), U_IS2.8 (VBUS), U_IS3.8 (VBUS), U_IS4.8 (VBUS), U_IS_MAIN.8 (VBUS), VDIS_LINK.2 (B)
- new net +3V3_BIAS_EN: R_EN_BIAS.2 (B), U_BEC_5V_1.10 (EN), U_BEC_5V_2.10 (EN), U_BEC_6V.3 (EN)
- new net +5V_AVIONICS: D_OR1.2 (K), D_OR1.3 (K2), D_OR2.2 (K), D_OR2.3 (K2), J_5V.1 (+), J_5V.2 (+)
- new net +5V_PRE_OR1: C_BEC1_OUT1.1 (P), C_BEC1_OUT2.1 (P), D_OR1.1 (A), L1.2 (B), R_FB1_1.1 (A)
- new net +5V_PRE_OR2: C_BEC2_OUT1.1 (P), C_BEC2_OUT2.1 (P), D_OR2.1 (A), L2.2 (B), R_FB2_1.1 (A)
- new net +6V_SERVO: C_BEC_SV_OUT1.1 (P), C_BEC_SV_OUT2.1 (P), J_6V.1 (+), J_6V.2 (+), L3.2 (B), R_FB6_1.1 (A)
- new net BATT_CM1_N: CM1.4 (P2B), CM2.3 (P2A)
- new net BATT_CM1_P: CM1.2 (P1B), CM2.1 (P1A)
- new net BATT_DSG_GATE: R_DSG_G.1 (A), U_CELL.1 (DSG)
- new net BATT_DSG_GATE_R: Q_BATT_DSG.4 (G), R_DSG_G.2 (B)
- new net BATT_RAW_N: CM1.3 (P2A), J_BATT.2 (-)
- new net BATT_RAW_P: CM1.1 (P1A), J_BATT.1 (+)
- new net BEC1_BOOT: C_BEC1_BOOT.1 (P), U_BEC_5V_1.13 (BOOT)
- new net BEC1_COMP: C_BEC1_COMP.1 (P), U_BEC_5V_1.8 (COMP)
- new net BEC1_FB: C_BEC1_COMP.2 (N), R_FB1_1.2 (B), R_FB1_2.1 (A), U_BEC_5V_1.7 (VSENSE)
- new net BEC1_SS: C_BEC1_SS.1 (P), U_BEC_5V_1.9 (SS/TR)
- new net BEC1_SW: C_BEC1_BOOT.2 (N), L1.1 (A), U_BEC_5V_1.11 (PH), U_BEC_5V_1.12 (PH)
- new net BEC2_BOOT: C_BEC2_BOOT.1 (P), U_BEC_5V_2.13 (BOOT)
- new net BEC2_COMP: C_BEC2_COMP.1 (P), U_BEC_5V_2.8 (COMP)
- new net BEC2_FB: C_BEC2_COMP.2 (N), R_FB2_1.2 (B), R_FB2_2.1 (A), U_BEC_5V_2.7 (VSENSE)
- new net BEC2_SS: C_BEC2_SS.1 (P), U_BEC_5V_2.9 (SS/TR)
- new net BEC2_SW: C_BEC2_BOOT.2 (N), L2.1 (A), U_BEC_5V_2.11 (PH), U_BEC_5V_2.12 (PH)
- new net BEC6_BOOT: C_BEC6_BOOT.1 (P), U_BEC_6V.1 (BOOT)
- new net BEC6_COMP: C_BEC6_COMP.1 (P), U_BEC_6V.6 (COMP)
- new net BEC6_FB: C_BEC6_COMP.2 (N), R_FB6_1.2 (B), R_FB6_2.1 (A), U_BEC_6V.5 (FB)
- new net BEC6_SW: C_BEC6_BOOT.2 (N), L3.1 (A), U_BEC_6V.8 (SW)
- new net CANFD_STB: R_CANSTB.1 (A), U_ISOCAN.4 (STB), U_MCU.27 (PA23/GPIO)
- new net CELL_ALERT_N: J_ALERT.2 (ALERT_N), R_ALERT.2 (B), U_CELL.30 (ALERT)
- new net CELL_B0: C_CAP1.2 (N), C_REGOUT.2 (N), J_BAL.1 (BAL_GND), U_CELL.27 (VC0)
- new net CELL_B1: R_BAL1.2 (B), U_CELL.26 (VC1)
- new net CELL_B2: R_BAL2.2 (B), U_CELL.25 (VC2)
- new net CELL_B3: R_BAL3.2 (B), U_CELL.24 (VC3)
- new net CELL_B4: R_BAL4.2 (B), U_CELL.23 (VC4)
- new net CELL_B5: C_CAP2.2 (N), R_BAL5.2 (B), U_CELL.10 (VC5x), U_CELL.21 (VC5B), U_CELL.22 (VC5)
- new net CELL_B6: R_BAL6.2 (B), U_CELL.16 (VC10), U_CELL.17 (VC9), U_CELL.18 (VC8), U_CELL.19 (VC7), U_CELL.20 (VC6)
- new net CELL_BAL1: J_BAL.2 (B1), R_BAL1.1 (A)
- new net CELL_BAL2: J_BAL.3 (B2), R_BAL2.1 (A)
- new net CELL_BAL3: J_BAL.4 (B3), R_BAL3.1 (A)
- new net CELL_BAL4: J_BAL.5 (B4), R_BAL4.1 (A)
- new net CELL_BAL5: J_BAL.6 (B5), R_BAL5.1 (A)
- new net CELL_BAL6: J_BAL.7 (B6), R_BAL6.1 (A)
- new net CELL_CAP1: C_CAP1.1 (P), U_CELL.7 (CAP1)
- new net CELL_CAP2: C_CAP2.1 (P), U_CELL.11 (NC), U_CELL.12 (NC), U_CELL.14 (CAP2)
- new net CELL_CHG_GATE: Q_BATT_CHG.4 (G), U_CELL.2 (CHG)
- new net CELL_REGOUT: C_REGOUT.1 (P), R_NTC_PU.1 (A), U_CELL.8 (REGOUT)
- new net ESC1_CM: CM_ESC1.2 (P1B), RS1.1 (IP), RS1.2 (IP)
- new net ESC1_OUT: ESC1_LINK.2 (B), J_ESC1.1 (+)
- new net ESC2_CM: CM_ESC2.2 (P1B), RS2.1 (IP), RS2.2 (IP)
- new net ESC2_OUT: ESC2_LINK.2 (B), J_ESC2.1 (+)
- new net ESC3_CM: CM_ESC3.2 (P1B), RS3.1 (IP), RS3.2 (IP)
- new net ESC3_OUT: ESC3_LINK.2 (B), J_ESC3.1 (+)
- new net ESC4_CM: CM_ESC4.2 (P1B), RS4.1 (IP), RS4.2 (IP)
- new net ESC4_OUT: ESC4_LINK.2 (B), J_ESC4.1 (+)
- new net GND: C_BEC1_IN.2 (N), C_BEC1_OUT1.2 (N), C_BEC1_OUT2.2 (N), C_BEC1_SS.2 (N), C_BEC2_IN.2 (N), C_BEC2_OUT1.2 (N), C_BEC2_OUT2.2 (N), C_BEC2_SS.2 (N), C_BEC_SV_IN.2 (N), C_BEC_SV_OUT1.2 (N), C_BEC_SV_OUT2.2 (N), C_ISOCAN1.2 (N), C_ISOCAN2.2 (N), C_ISOCAN3.2 (N), C_RS485_1.2 (N), C_RS485_2.2 (N), C_RS485_3.2 (N), C_TPM1.2 (N), C_TPM2.2 (N), C_TPM3.2 (N), C_TPM4.2 (N), J_5V.3 (-), J_5V.4 (-), J_6V.3 (-), J_6V.4 (-), R_CANSTB.2 (B), R_FB1_2.2 (B), R_FB2_2.2 (B), R_FB6_2.2 (B), R_GND_PGND.1 (A), U_BEC_5V_1.1 (RT/CLK), U_BEC_5V_1.15 (EP), U_BEC_5V_1.2 (GND), U_BEC_5V_1.3 (GND), U_BEC_5V_2.1 (RT/CLK), U_BEC_5V_2.15 (EP), U_BEC_5V_2.2 (GND), U_BEC_5V_2.3 (GND), U_BEC_6V.4 (RT/CLK), U_BEC_6V.7 (GND), U_BEC_6V.9 (EP), U_IS1.1 (A1), U_IS1.2 (A0), U_IS1.7 (GND), U_IS2.1 (A1), U_IS2.7 (GND), U_IS3.1 (A1), U_IS3.7 (GND), U_IS4.1 (A1), U_IS4.7 (GND), U_ISOCAN.10 (GND1), U_ISOCAN.6 (GNDIO), U_IS_MAIN.2 (A0), U_IS_MAIN.7 (GND), U_RS485.10 (GND1), U_RS485.6 (GNDIO)
- new net I2C_SCL: D_I2C.1 (IO1), J_I2C.3 (SCL), R_I2C_SCL.2 (B), U_CELL.5 (SCL), U_IS1.5 (SCL), U_IS2.5 (SCL), U_IS3.5 (SCL), U_IS4.2 (A0), U_IS4.5 (SCL), U_IS_MAIN.5 (SCL), U_MCU.2 (PA1/I2C0_SCL)
- new net I2C_SDA: D_I2C.3 (IO2), J_I2C.4 (SDA), R_I2C_SDA.2 (B), U_CELL.4 (SDA), U_IS1.4 (SDA), U_IS2.4 (SDA), U_IS3.2 (A0), U_IS3.4 (SDA), U_IS4.4 (SDA), U_IS_MAIN.4 (SDA), U_MCU.1 (PA0/I2C0_SDA)
- new net ISO_5V_485: C_RS485_4.1 (P), C_RS485_5.1 (P), U_RS485.12 (VISOOUT), U_RS485.16 (VISOIN)
- new net J_CHASSIS_NET: C_Y1.2 (N), C_Y2.2 (N), J_CHASSIS.1 (PGND), R_CHGND.1 (A)
- new net REG3V3_SW: L_H1.1 (A), U_REG_3V3_H.3 (SW)
- new net SHUNT1_N: ESC1_LINK.1 (A), RS1.4 (SN), U_IS1.9 (IN-)
- new net SHUNT1_P: RS1.3 (SP), U_IS1.10 (IN+)
- new net SHUNT2_N: ESC2_LINK.1 (A), RS2.4 (SN), U_IS2.9 (IN-)
- new net SHUNT2_P: RS2.3 (SP), U_IS2.10 (IN+)
- new net SHUNT3_N: ESC3_LINK.1 (A), RS3.4 (SN), U_IS3.9 (IN-)
- new net SHUNT3_P: RS3.3 (SP), U_IS3.10 (IN+)
- new net SHUNT4_N: ESC4_LINK.1 (A), RS4.4 (SN), U_IS4.9 (IN-)
- new net SHUNT4_P: RS4.3 (SP), U_IS4.10 (IN+)
- new net SHUNT_MAIN_N: RS_MAIN.4 (SN), U_CELL.29 (SRN), U_IS_MAIN.9 (IN-), VDIS_LINK.1 (A)
- new net SHUNT_MAIN_P: RS_MAIN.3 (SP), U_CELL.28 (SRP), U_IS_MAIN.10 (IN+)
- new net TPM_P10_PU: R_TPM10.2 (B), U_TPM.10 (NCI/VDD)
- new net VBAT_F1: C1.1 (P), C2.1 (P), C3.1 (P), C_DM1.1 (P), C_Y1.1 (P), D1.1 (A), F1.2 (B), RS_MAIN.1 (IP), RS_MAIN.2 (IP)
- new net VDIS_5V1: C_BEC1_IN.1 (P), FB_5V1.2 (OUT)
- new net VDIS_5V2: C_BEC2_IN.1 (P), FB_5V2.2 (OUT)
- new net VDIS_6V: C_BEC_SV_IN.1 (P), FB_6V.2 (OUT)
- no-connect marks 83 -> 32
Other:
- note removed: "=== Section A: Battery Input / Main Bus Filter ==="
- note removed: "=== Section B: Battery Disconnect + Main Shunt ==="
- note removed: "=== Section C: ESC Power Branches (x4) ==="
- note removed: "=== Section D: Dual 5V BEC (diode-OR) ==="
- note removed: "=== Section E: 5V Servo BEC (Rev S1 - 6V BEC retired) ==="
- note removed: "=== Section F: BQ76930 6S Cell Monitor ==="
- note removed: "=== Section G: I2C Interface, TVS, Alert, Connectors ==="
- note removed: "=== Section H: Trust Module (MCU+TPM+isolated CAN-FD+RS-485) ==="
- note removed: "ESC5 branch: DNP — Phase 11 only"
- title: FlightEngineer — EMI-Hardened Power Distribution Board -> Flight Engineer — Power Distribution Board

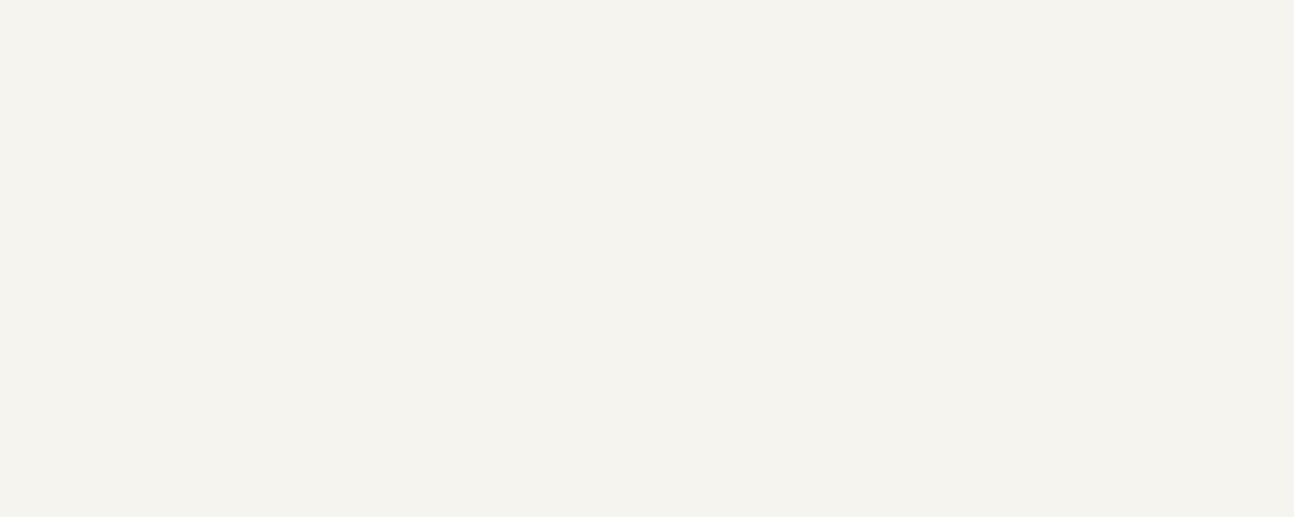
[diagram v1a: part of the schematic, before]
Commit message: docs(avionics): Wurth usage notice + uncrewed-only statement on 5 boards; catalogue REF-SENSOR-022..040
Owner decision 2026-09-26: retain the Wurth parts. The Wurth datasheet
usage notice is quoted verbatim [REF-SENSOR-028: Wurth 749010012A data
sheet rev 004.000 p.1] with an 'intended for use only on uncrewed
aircraft' statement in each Wurth-bearing board's .md, as a schematic
text item and PCB Cmts.User text, and in title-block comments 8/9
(tools/add_board_notices.py, idempotent). ERC/DRC/parity counts
unchanged on all five boards (kicad-cli 9.0.2).

REFERENCES.md: REF-SENSOR-022/023/025-030/033/038/040 were cited by
board schematics and generator scripts but never catalogued; entries
added with URLs validated 2026-09-26, unreachable ones marked
'requires verification'.

AI-authored: Claude Opus 5.5 (Anthropic).

Co-Authored-By: Claude Opus 5.5 <noreply@anthropic.com>
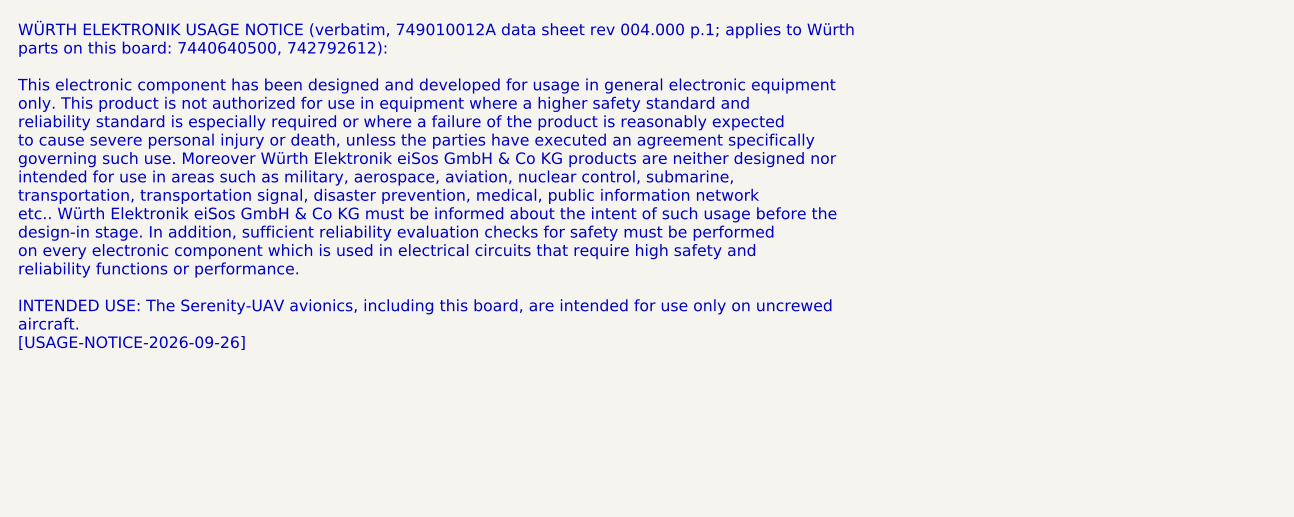
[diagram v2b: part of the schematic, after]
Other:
- note added: "WÜRTH ELEKTRONIK USAGE NOTICE (verbatim, 749010012A data sheet rev 004.000 p.1; applies to Würth parts on this board: 7440640500, 742792612): This electronic component has been designed and developed for usage in general electronic equipment only. This product is not authorized for use in equipment where a higher safety standard and reliability standard is especially required or where a failure o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"
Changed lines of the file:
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@@
     (comment 3 "Author: Claude Sonnet 5 (2026-09-20); owner sgriffing")
     (comment 4 "CC BY 4.0 — pinouts transcribed from OEM datasheets in avionics/datasheets/")
-  )
+		(comment 8 "Wurth parts (7440640500, 742792612): see Wurth usage notice on this page [USAGE-NOTICE-2026-09-26]")
+		(comment 9 "Intended for use ONLY on uncrewed aircraft")
+	)
   (symbol (lib_id "FlightEngineer:S_U_IS_MAIN") (at 76.20 86.36 0) (unit 1)
     (exclude_from_sim no) (in_bom yes) (on_board yes) (dnp no)
@@
   (wire (pts (xy 320.04 30.48) (xy 320.04 33.02)) (stroke (width 0) (type default)))
   (global_label "J_CHASSIS_NET" (shape passive) (at 320.04 33.02 270) (effects (font (size 1.27 1.27)) (justify right)))
-  (sheet_instances (path "/" (page "1")))
+	(text "WÜRTH ELEKTRONIK USAGE NOTICE (verbatim, 749010012A data sheet rev 004.000 p.1; applies to Würth\nparts on this board: 7440640500, 742792612):\n\nThis electronic component has been designed and developed for usage in general electronic equipment\nonly. This product is not authorized for use in equipment where a higher safety standard and\nreliability standard is especially required or where a failure of the product is reasonably expected\nto cause severe personal injury or death, unless the parties have executed an agreement specifically\ngoverning such use. Moreover Würth Elektronik eiSos GmbH & Co KG products are neither designed nor\nintended for use in areas such as military, aerospace, aviation, nuclear control, submarine,\ntransportation, transportation signal, disaster prevention, medical, public information network\netc.. Würth Elektronik eiSos GmbH & Co KG must be informed about the intent of such usage before the\ndesign-in stage. In addition, sufficient reliability evaluation checks for safety must be performed\non every electronic component which is used in electrical circuits that require high safety and\nreliability functions or performance.\n\nINTENDED USE: The Serenity-UAV avionics, including this board, are intended for use only on uncrewed\naircraft.\n[USAGE-NOTICE-2026-09-26]"
+		(exclude_from_sim no)
+		(at -20.32 -86.36 0)
+		(effects (font (size 1.27 1.27)) (justify left top))
+	)
+	(sheet_instances (path "/" (page "1")))
 )
